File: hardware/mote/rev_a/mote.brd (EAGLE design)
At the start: 160 x 100 mm, 139 parts, among them J1 TC2030-JLINK-L, J2 TC2030-JLINK-L, Q1 CSD22206W, Q10 CSD22206W, Q11 CSD22206W, Q2 CSD22206W, Q6 CSD22206W, Q7 CSD22206W, Q8 CSD22206W, Q9 CSD22206W, U1 NRF52840, U10 MS5637-02BA03, U11 ADP5091, U12 NRF51822QF, U3 MAX17222, U4 AMN41121, U5 SI7021-A20-GM1, U6 ISL29125, U7 MAX44009, U8 LIS2DW12, U9 AB1815-T3, X1 7V-32.000MAHV-T, X2 ABS05-32.768KHZ-9-T, X3 ABS07-32.768KHZ-7-T, X5 16MHz, X6 ABS05-32.768KHZ-9-T

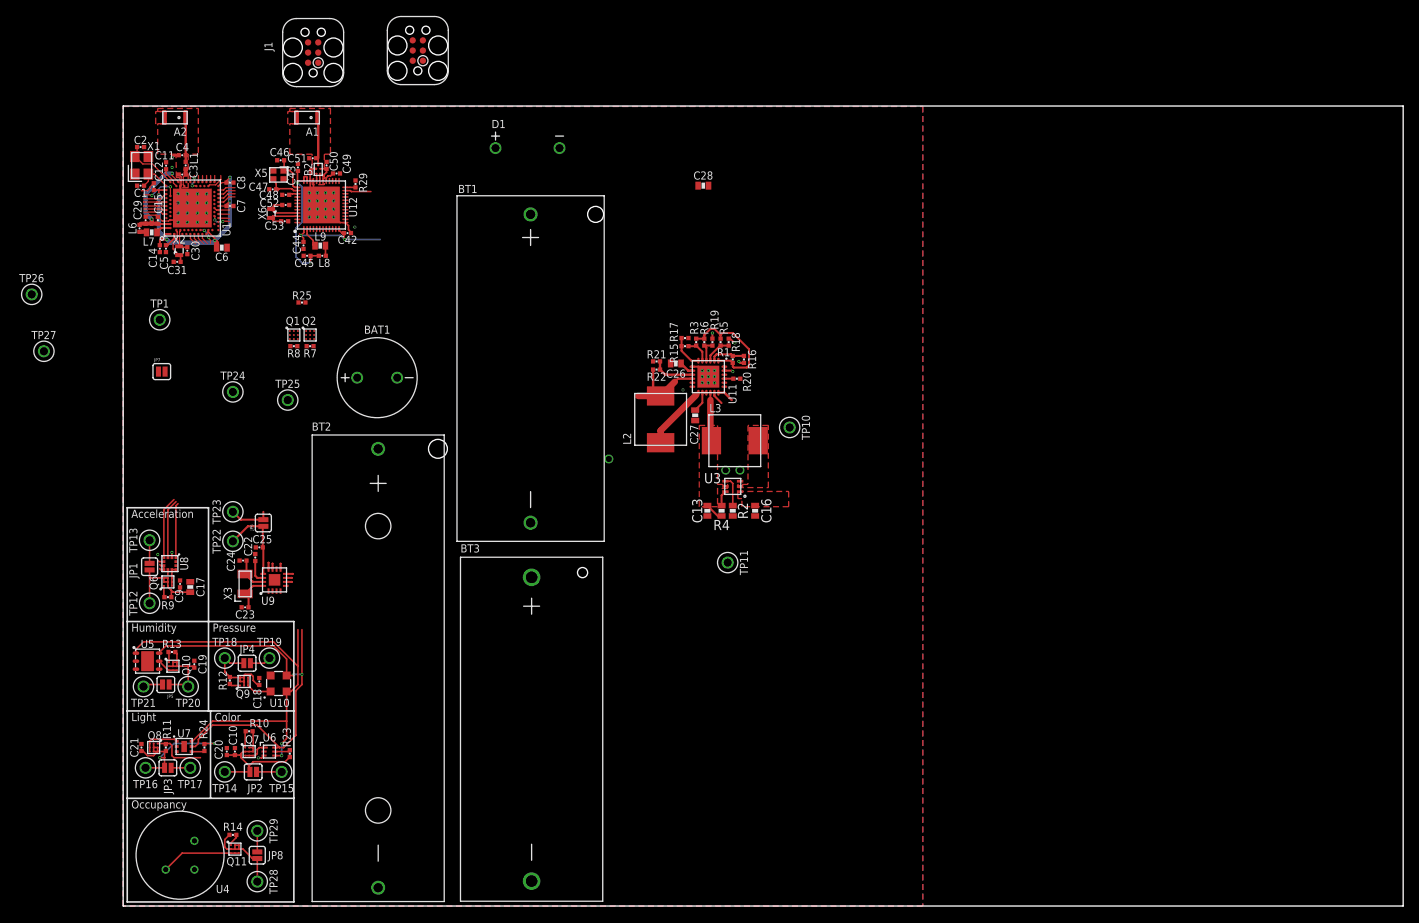
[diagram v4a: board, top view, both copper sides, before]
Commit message: Rearrange sensors, current measurement
Ready for signal routing!
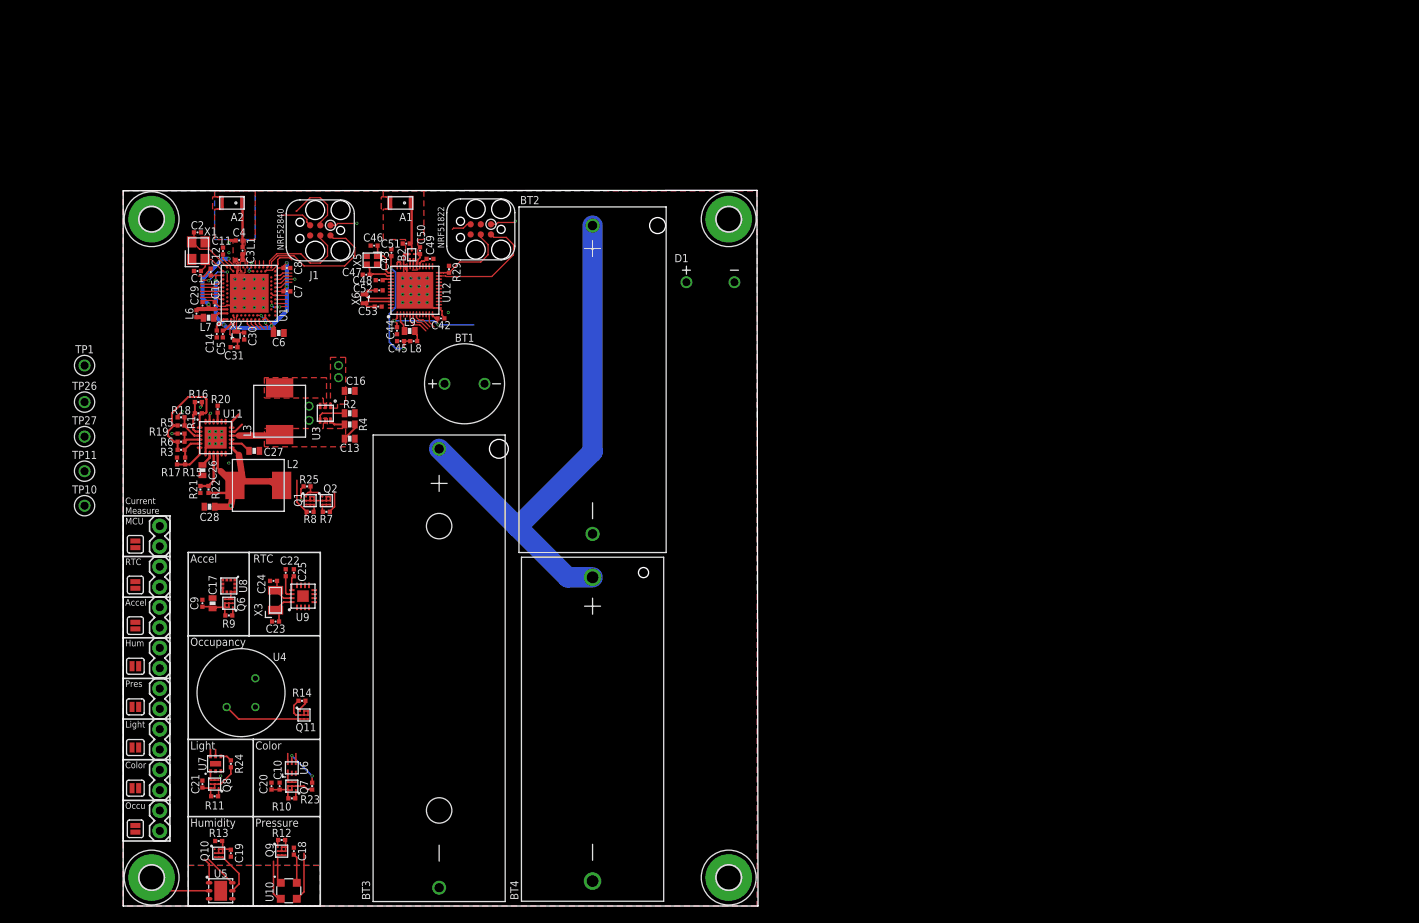
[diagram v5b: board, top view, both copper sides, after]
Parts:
- removed BAT1: LTOHTC1020, batteries:1020
- removed TP12, TP13, TP14, TP15, TP16, TP17, TP18, TP19, TP20, TP21, TP22, TP23, TP24, TP25, TP28, TP29: TEST_POINT_0.040IN, headers:TESTPOINT_0.040IN
- added BT4: BAT_PACKCR123A, batteries:BH123A
- added H1, H2, H3, H4: MOUNT-PAD-ROUND3.0, holes:3,0-PAD
- added JP10, JP11, JP12, JP13, JP14, JP15, JP16, JP9: (no value), SparkFun-Connectors:1X02
- BT1: value BAT_PACK2/3AA -> LTOHTC1020; device batteries:6S-2-3A -> batteries:1020
- BT2: value BAT_PACKAA -> BAT_PACK2/3AA; device batteries:BHAA-3 -> batteries:6S-2-3A
- BT3: value BAT_PACKCR123A -> BAT_PACKAA; device batteries:BH123A -> batteries:BHAA-3
- moved TP10 88.7 mm to (-4.83, 50.0), turned to 180 degrees
- moved TP11 81.2 mm to (-4.83, 54.4), turned to 0 degrees
- moved C28 73.6 mm to (10.8, 49.9), turned to 180 degrees
- moved R18 69.1 mm to (7.24, 61.1), turned to 0 degrees
- moved R16 68.4 mm to (9.40, 63.0), turned to 180 degrees
- moved R5 68.2 mm to (7.24, 60.1), turned to 180 degrees
- moved R19 67.4 mm to (7.24, 59.1), turned to 0 degrees
- moved R1 67.1 mm to (9.40, 61.6), turned to 0 degrees
- moved R6 66.6 mm to (7.24, 58.0), turned to 180 degrees
- moved R3 65.8 mm to (7.24, 57.0), turned to 180 degrees
- moved R17 65.3 mm to (6.73, 55.6), turned to 270 degrees
- moved R20 65.0 mm to (11.8, 62.1), turned to 270 degrees
- moved R15 64.1 mm to (7.75, 55.6), turned to 90 degrees
- moved U11 62.1 mm to (11.6, 58.5), turned to 0 degrees
- moved C26 60.7 mm to (9.91, 54.5), turned to 270 degrees
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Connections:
- removed net N$39: C12.1, C14.1, C6.1, C7.1, C8.1, JP7.1, TP24.TESTPOINT, U1.A22, U1.AD14, U1.AD23, U1.B1, U1.W1, U1.Y2
- removed net NRF_VCC: C42.1, C44.1, J2.1, U12.1, U12.12
- new net VCC_JUMP: C12.1, C14.1, C42.1, C44.1, C6.1, C7.1, C8.1, JP7.1, JP9.1, U1.A22, U1.AD14, U1.AD23, U1.B1, U1.W1, U1.Y2, U12.1, U12.12
- net GND: now also BT4.-, H1.B3,0, H2.B3,0, H3.B3,0, H4.B3,0; no longer BAT1.-
- net N$19: now also JP15.1; no longer TP18.TESTPOINT
- net N$24: now also JP14.1; no longer TP28.TESTPOINT
- net N$33: now also JP12.1; no longer TP14.TESTPOINT
- net N$36: now also JP16.1; no longer TP20.TESTPOINT
- net N$37: now also JP13.1; no longer TP16.TESTPOINT
- net N$40: now also JP11.1; no longer TP12.TESTPOINT
- net N$42: now also JP10.1; no longer TP22.TESTPOINT
- net VBAT: now also BT4.+, JP10.2; no longer BT1.+, TP23.TESTPOINT
- net VCC: now also J2.1, JP11.2, JP12.2, JP13.2, JP14.2, JP15.2, JP16.2, JP9.2; no longer TP13.TESTPOINT, TP15.TESTPOINT, TP17.TESTPOINT, TP19.TESTPOINT, TP21.TESTPOINT, TP25.TESTPOINT, TP29.TESTPOINT
- net VSEC: now also BT1.+; no longer BAT1.+
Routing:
- net VBAT: track 7.26 -> 72.3 mm
- net VCC_JUMP: track 0.00 -> 47.2 mm, vias 0 -> 7
- net SDA: track 54.5 -> 16.8 mm, vias 2 -> 0
- net SCL: track 52.9 -> 16.6 mm, vias 2 -> 0
- net N$39: track 32.9 -> 0.00 mm, vias 5 -> 0
- net N$28: track 0.83 -> 17.2 mm
- net GND: track 33.3 -> 48.2 mm, vias 54 -> 52
- net NRF_VCC: track 14.3 -> 0.00 mm, vias 2 -> 0
- net N$37: track 20.1 -> 7.00 mm, vias 2 -> 0
- net NRF_SWDIO/!RESET: track 3.23 -> 15.1 mm
- net N$29: track 0.83 -> 12.3 mm
- net N$33: track 17.9 -> 7.84 mm
- net N$42: track 10.8 -> 1.86 mm
- net NRF_SWDCLK: track 1.26 -> 9.99 mm
- net N$19: track 12.1 -> 3.42 mm
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- added copper zone on layer 2, net GND
- added copper zone on layer 15, net N$35
- added copper zone on layer 16, net N$39
- added copper zone on layer 1, net N$43
- added copper zone on layer 15, net N$43
- added copper zone on layer 16, net N$43
- added copper zone on layer 2, net N$43
- added copper zone on layer 2, net N$7
- added copper zone on layer 15, net VCC
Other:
- board size 160 x 100 mm -> 79.4 x 89.5 mm
- board text added: "Accel"
- board text added: "Current Measure"
- board text added: "Hum"
- board text added: "MCU"
- board text added: "NRF51822"
- board text added: "NRF52840"
- board text added: "Occu"
- board text added: "Pres"
- board text added: "RTC"
- board text removed: "Acceleration"

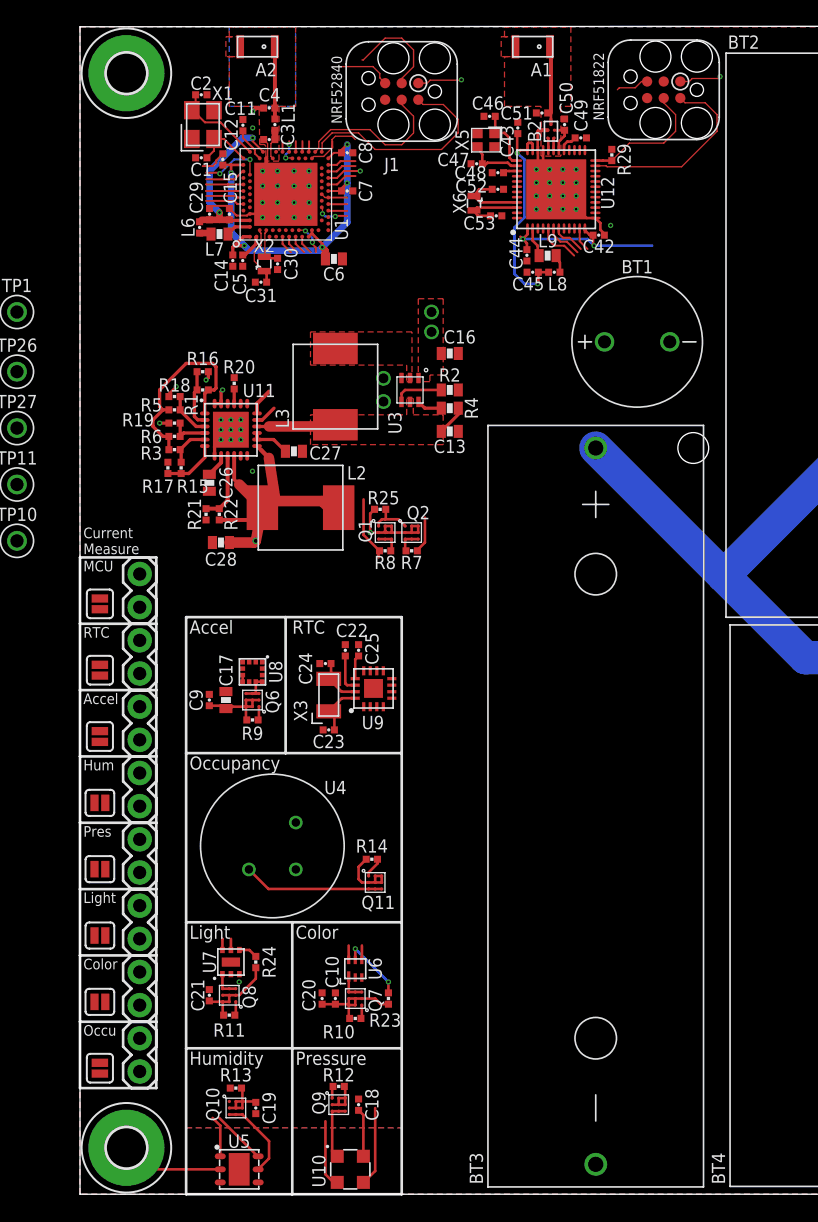
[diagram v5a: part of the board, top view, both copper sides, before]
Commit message: Route I2C, sensor power pins
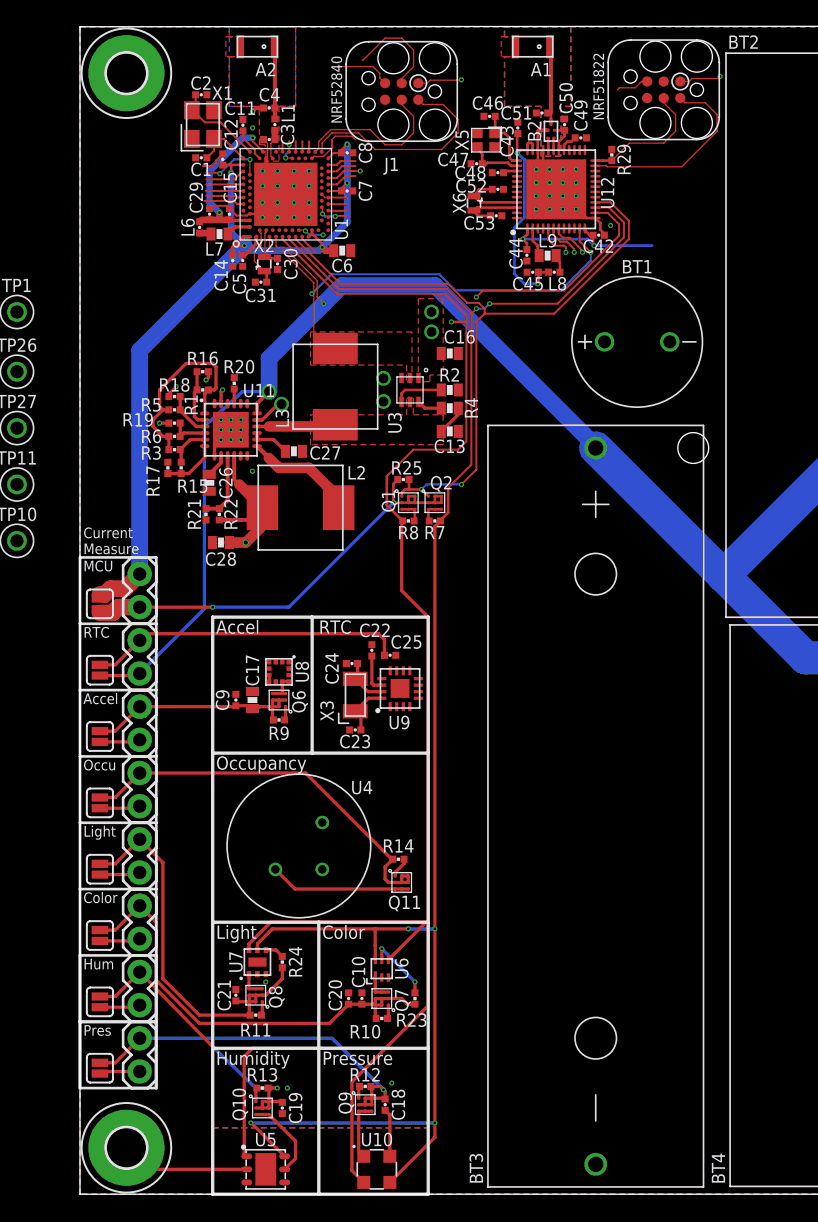
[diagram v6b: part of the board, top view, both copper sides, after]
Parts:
- moved JP14 20.3 mm to (4.57, 32.3)
- moved JP8 20.3 mm to (1.52, 30.0), turned to 270 degrees
- moved JP16 15.2 mm to (4.57, 17.0)
- moved JP5 15.2 mm to (1.52, 14.7), turned to 270 degrees
- moved JP15 15.2 mm to (4.57, 11.9)
- moved JP4 15.2 mm to (1.52, 9.65), turned to 270 degrees
- moved JP13 5.08 mm to (4.57, 27.2)
- moved JP2 5.08 mm to (1.52, 19.8), turned to 270 degrees
- moved JP12 5.08 mm to (4.57, 22.1)
- moved JP3 5.08 mm to (1.52, 24.9), turned to 270 degrees
- moved Q1 2.90 mm to (25.1, 53.0)
- moved Q2 2.90 mm to (27.2, 53.0)
- moved R25 2.90 mm to (24.8, 54.7)
- moved R7 2.90 mm to (27.2, 51.6)
- moved R8 2.90 mm to (25.1, 51.6)
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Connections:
- net !I2C_EN: now also U1.R1, U12.16; no longer U1.B19, U12.21
- net !PR_EN: now also U1.B19; no longer U1.R1
- net ACC_CS: now also U12.20; no longer U12.19
- net MISO: now also U12.17; no longer U12.16
- net MOSI: now also U12.18; no longer U12.17
- net RTC_CS: now also U12.21; no longer U12.20
- net SCK: now also U12.19; no longer U12.18
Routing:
- net SDA: track 16.8 -> 150.1 mm, vias 0 -> 2
- net SCL: track 16.6 -> 138.2 mm, vias 0 -> 6
- net VSOL: track 18.7 -> 111.2 mm, vias 1 -> 2
- net VBAT: track 72.3 -> 161.5 mm, vias 0 -> 3
- net VCC_JUMP: track 47.2 -> 94.8 mm
- net !I2C_EN: track 8.41 -> 55.6 mm
- net VCC: track 15.3 -> 59.9 mm, vias 5 -> 6
- net VSEC: track 7.92 -> 44.0 mm, vias 0 -> 2
- net SW: track 1.82 -> 36.0 mm, vias 0 -> 2
- net N$19: track 3.42 -> 30.4 mm, vias 0 -> 1
- net N$33: track 7.84 -> 34.6 mm
- net N$24: track 5.14 -> 31.1 mm
- net N$37: track 7.00 -> 30.6 mm
- net N$42: track 1.86 -> 24.2 mm
- net N$36: track 4.60 -> 23.4 mm, vias 0 -> 2
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- added copper zone on layer 15, net N$38
- added copper zone on layer 16, net N$38
- added copper zone on layer 2, net N$38

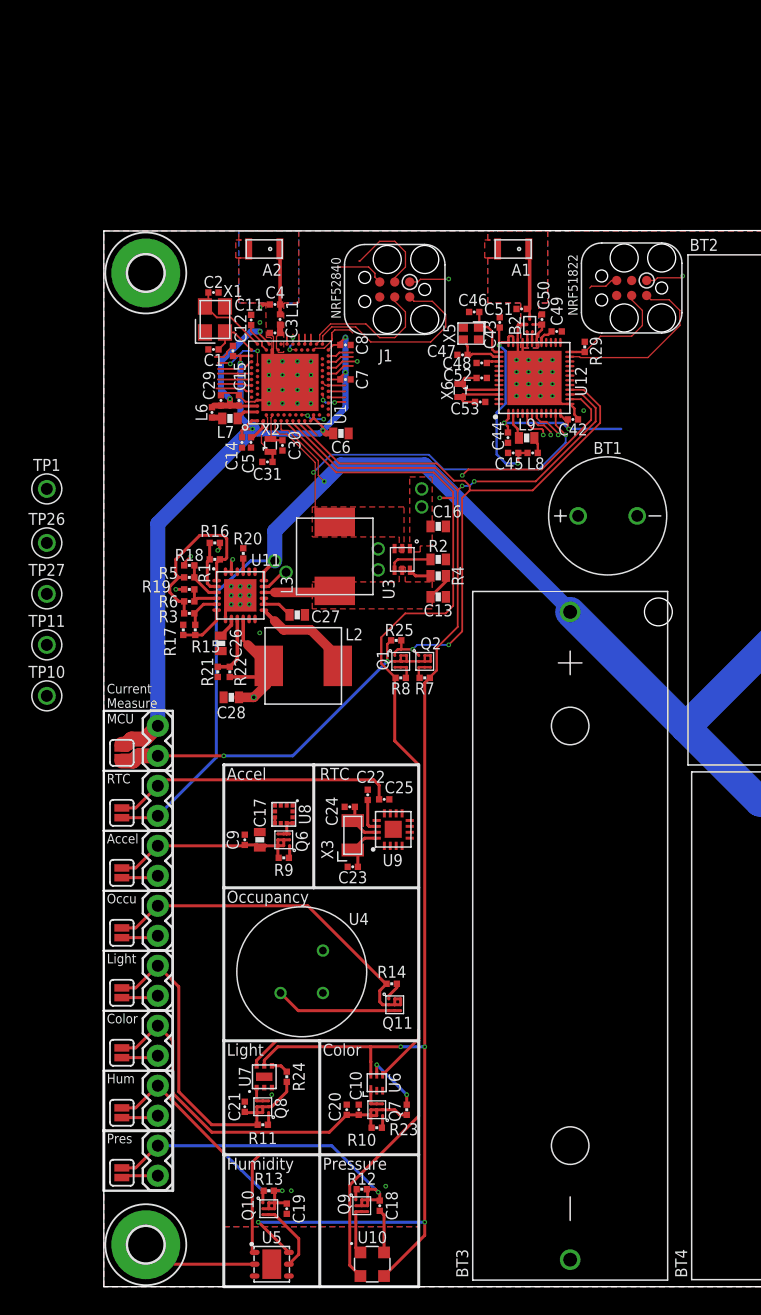
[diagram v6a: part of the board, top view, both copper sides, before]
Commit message: Majority of signals routed
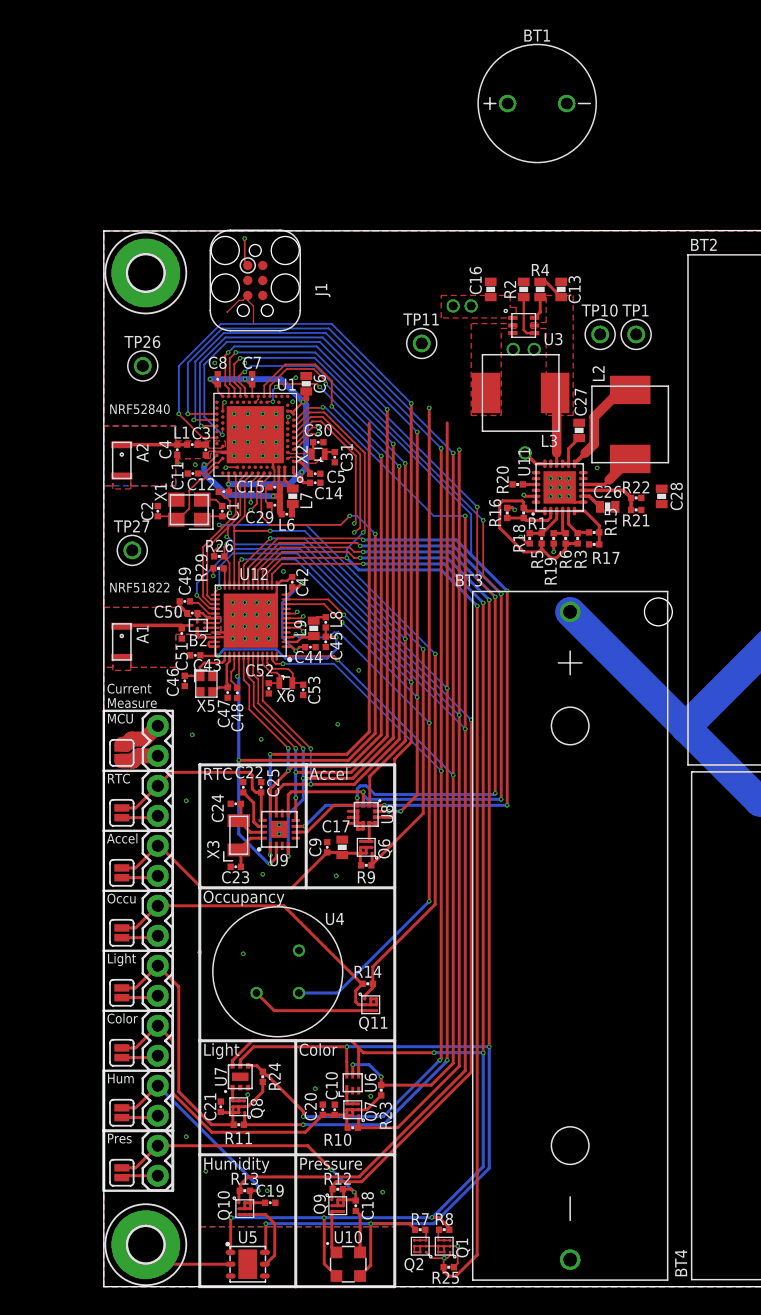
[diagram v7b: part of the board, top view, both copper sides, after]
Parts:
- removed J2: TC2030-JLINK-L, connector:TC2030-IDC
- added R26: 150, passives:0402_RES
- moved TP10 56.0 mm to (42.0, 80.6)
- moved R25 53.3 mm to (29.2, 1.65), turned to 0 degrees
- moved TP1 51.6 mm to (45.1, 80.6)
- moved Q1 49.7 mm to (28.8, 3.43), turned to 180 degrees
- moved Q2 49.5 mm to (26.8, 3.43), turned to 180 degrees
- moved A1 47.0 mm to (1.52, 54.6), turned to 270 degrees
- moved R8 46.9 mm to (28.8, 4.83), turned to 180 degrees
- moved R7 46.7 mm to (26.8, 4.83), turned to 0 degrees
- moved TP11 40.7 mm to (26.9, 79.9)
- moved C28 40.2 mm to (47.2, 66.9), turned to 270 degrees
- moved C51 39.8 mm to (6.60, 55.3), turned to 270 degrees
- moved C46 39.7 mm to (6.86, 51.3), turned to 270 degrees
- moved C49 38.9 mm to (6.86, 58.0), turned to 180 degrees
- moved C50 38.7 mm to (7.49, 57.0), turned to 180 degrees
- moved C43 38.2 mm to (7.75, 53.5), turned to 180 degrees
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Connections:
- removed net N$28: J1.2, U1.AC24
- removed net N$29: J1.4, U1.AA24
- removed net NRF_SWDCLK: J2.4, R29.1, U12.24
- removed net NRF_SWDIO/!RESET: J2.2, J2.6, U12.23
- new net SWDCLK: J1.4, R29.1, U1.AA24, U12.24
- new net SWDIO: J1.2, J1.6, R26.2, U1.AC24, U12.23
- net !CLR_EN: now also U12.25; no longer U12.26
- net !HUM_EN: now also U12.21; no longer U12.40
- net !I2C_EN: now also U12.15; no longer U12.16
- net !LT_EN: now also U12.26; no longer U12.25
- net !RST: now also R26.1
- net !RTC_IRQ1: now also U12.44; no longer U12.41
- net !RTC_IRQ2: now also U12.43; no longer U12.42
- net !RTC_IRQ3: now also U12.42
- net ACC_INT1: now also U12.10; no longer U12.43
- net ACC_INT2: now also U12.11; no longer U12.44
- net GND: no longer J2.5
- net RTC_CS: now also U12.41; no longer U12.21
- net SCL: now also U12.16; no longer U12.15
- net SW: now also U12.8; no longer U12.11
- net VCC: no longer J2.1
- net WDI: now also U1.A8, U12.40
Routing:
- net !LT_INT: track 2.28 -> 123.6 mm, vias 0 -> 6
- net !HUM_EN: track 2.67 -> 117.7 mm, vias 0 -> 4
- net !CLR_INT: track 6.10 -> 116.9 mm, vias 2 -> 6
- net !LT_EN: track 3.92 -> 111.9 mm, vias 0 -> 4
- net !CLR_EN: track 3.06 -> 109.1 mm, vias 2 -> 4
- net VSOL: track 111.2 -> 9.96 mm
- net MOSI: track 2.25 -> 101.6 mm, vias 0 -> 6
- net MISO: track 2.20 -> 99.3 mm, vias 0 -> 6
- net SCK: track 2.67 -> 96.0 mm, vias 1 -> 6
- net !PR_EN: track 5.93 -> 93.9 mm, vias 2 -> 3
- net PIR_OUT: track 4.90 -> 90.5 mm, vias 0 -> 5
- net VBAT: track 161.5 -> 76.8 mm
- net ACC_INT2: track 0.82 -> 82.7 mm, vias 0 -> 4
- net ACC_INT1: track 0.82 -> 78.6 mm, vias 0 -> 6
- net !RTC_IRQ3: track 1.92 -> 78.1 mm, vias 2 -> 5
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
